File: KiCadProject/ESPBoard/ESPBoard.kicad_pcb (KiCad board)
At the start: 2 copper layers, 45 x 45 mm, 1 part, among them U301 ESP32-S3-WROOM-1

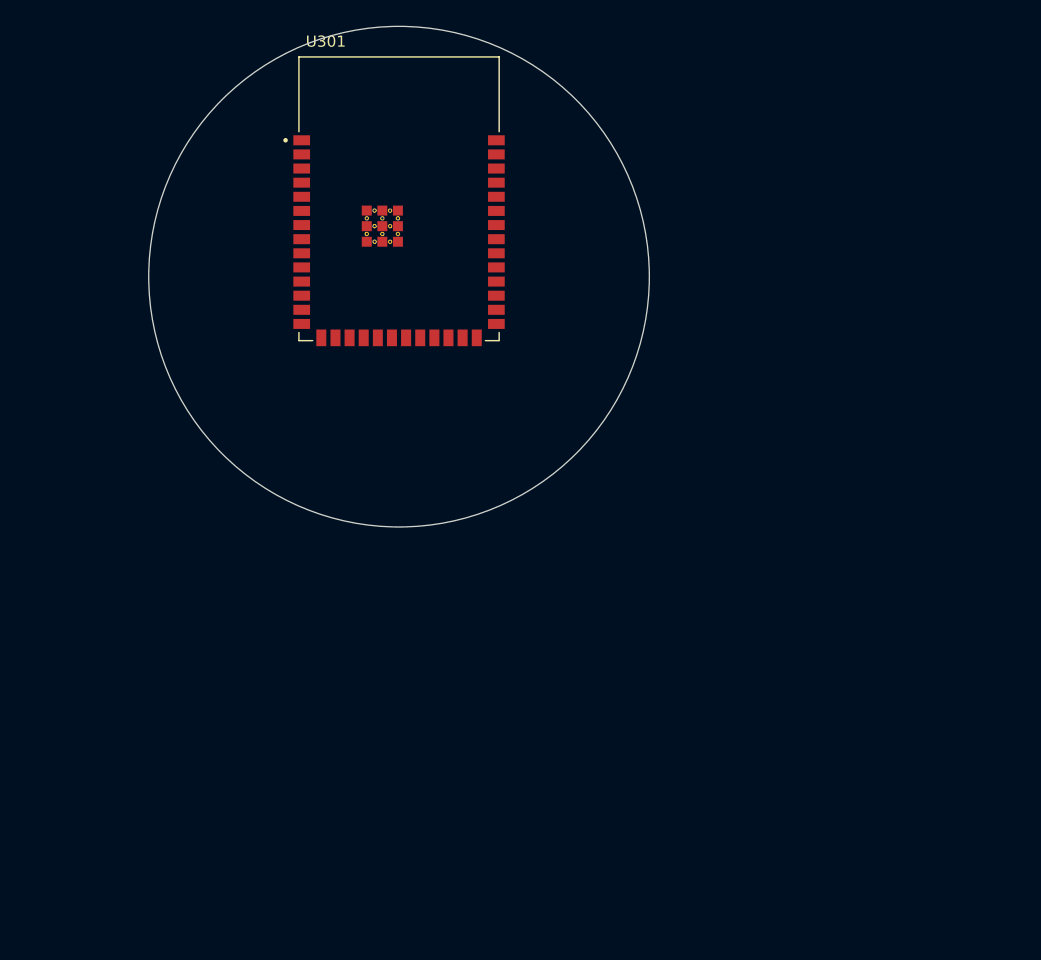
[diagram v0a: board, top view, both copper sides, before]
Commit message: ESP board layout mostly done. Small updates to battery management board
Signed-off-by: Eldalote.Electronics <Eldalote.Electronics@gmail.com>
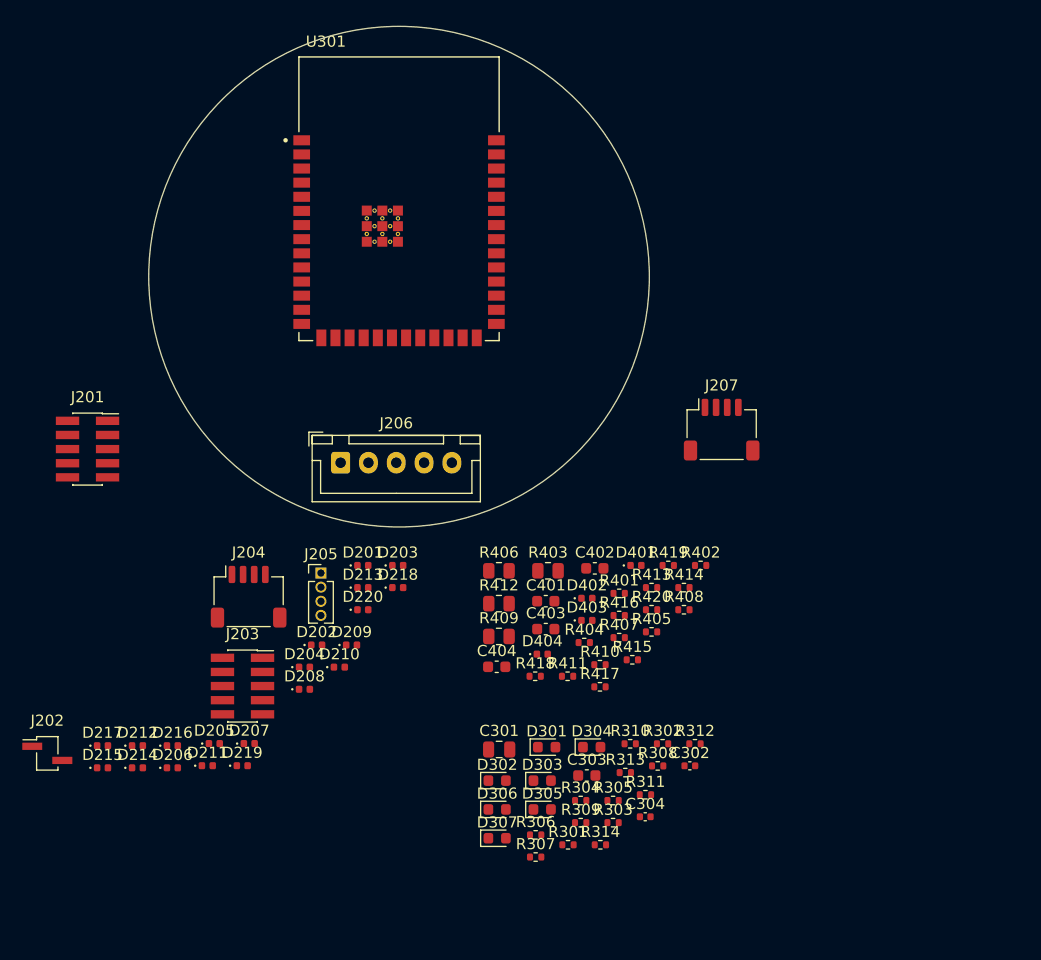
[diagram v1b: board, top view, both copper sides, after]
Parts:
- added C301: 10u, Capacitor_SMD:C_0805_2012Metric, F.Cu at (159.0, 142.5)
- added C302: 100n, Capacitor_SMD:C_0402_1005Metric, F.Cu at (176.1, 144.0)
- added C303: 1u, Capacitor_SMD:C_0603_1608Metric, F.Cu at (166.9, 144.8)
- added C304: 100n, Capacitor_SMD:C_0402_1005Metric, F.Cu at (172.1, 148.6)
- added C401: 1u, Capacitor_SMD:C_0603_1608Metric, F.Cu at (163.2, 129.2)
- added C402: 1u, Capacitor_SMD:C_0603_1608Metric, F.Cu at (167.6, 126.2)
- added C403: 1u, Capacitor_SMD:C_0603_1608Metric, F.Cu at (163.2, 131.7)
- added C404: 1u, Capacitor_SMD:C_0603_1608Metric, F.Cu at (158.8, 135.1)
- added D201: 3v3, Diode_SMD:D_0402_1005Metric, F.Cu at (146.7, 126.0)
- added D202: 3v3, Diode_SMD:D_0402_1005Metric, F.Cu at (142.6, 133.1)
- added D203: 3v3, Diode_SMD:D_0402_1005Metric, F.Cu at (149.9, 126.0)
- added D204: 3v3, Diode_SMD:D_0402_1005Metric, F.Cu at (141.5, 135.1)
- added D205: 3v3, Diode_SMD:D_0402_1005Metric, F.Cu at (133.4, 142.0)
- added D206: 3v3, Diode_SMD:D_0402_1005Metric, F.Cu at (129.6, 144.2)
- added D207: 3v3, Diode_SMD:D_0402_1005Metric, F.Cu at (136.5, 142.0)
- added D208: 3v3, Diode_SMD:D_0402_1005Metric, F.Cu at (141.5, 137.1)
- added D209: 3v3, Diode_SMD:D_0402_1005Metric, F.Cu at (145.7, 133.1)
- added D210: 3v3, Diode_SMD:D_0402_1005Metric, F.Cu at (144.6, 135.1)
- added D211: 3v3, Diode_SMD:D_0402_1005Metric, F.Cu at (132.8, 144.0)
- added D212: 3v3, Diode_SMD:D_0402_1005Metric, F.Cu at (126.5, 142.2)
- added D213: 3v3, Diode_SMD:D_0402_1005Metric, F.Cu at (146.7, 128.0)
- added D214: 3v3, Diode_SMD:D_0402_1005Metric, F.Cu at (126.5, 144.2)
- added D215: 3v3, Diode_SMD:D_0402_1005Metric, F.Cu at (123.3, 144.2)
- added D216: 3v3, Diode_SMD:D_0402_1005Metric, F.Cu at (129.6, 142.2)
- added D217: 3v3, Diode_SMD:D_0402_1005Metric, F.Cu at (123.3, 142.2)
- added D218: 3v3, Diode_SMD:D_0402_1005Metric, F.Cu at (149.9, 128.0)
- added D219: 3v3, Diode_SMD:D_0402_1005Metric, F.Cu at (135.9, 144.0)
- added D220: 3v3, Diode_SMD:D_0402_1005Metric, F.Cu at (146.7, 129.9)
- added D301: RED LED, LED_SMD:LED_0603_1608Metric, F.Cu at (163.3, 142.3)
- added D302: ORANGE LED, LED_SMD:LED_0603_1608Metric, F.Cu at (158.8, 145.3)
- added D303: GREEN LED, LED_SMD:LED_0603_1608Metric, F.Cu at (162.9, 145.3)
- added D304: GREEN LED, LED_SMD:LED_0603_1608Metric, F.Cu at (167.3, 142.3)
- added D305: GREEN LED, LED_SMD:LED_0603_1608Metric, F.Cu at (162.9, 147.9)
- added D306: GREEN LED, LED_SMD:LED_0603_1608Metric, F.Cu at (158.8, 147.9)
- added D307: GREEN LED, LED_SMD:LED_0603_1608Metric, F.Cu at (158.8, 150.5)
- added D401: 3v3, Diode_SMD:D_0402_1005Metric, F.Cu at (171.3, 126.0)
- added D402: 3v3, Diode_SMD:D_0402_1005Metric, F.Cu at (166.9, 128.9)
- added D403: 3v3, Diode_SMD:D_0402_1005Metric, F.Cu at (166.9, 130.9)
- added D404: 3v3, Diode_SMD:D_0402_1005Metric, F.Cu at (162.9, 133.9)
- added J201: Conn_02x05, Connector_PinSocket_1.27mm:PinSocket_2x05_P1.27mm_Vertical_SMD, F.Cu at (122.0, 115.5)
- added J202: Conn_01x02, Connector_PinSocket_1.27mm:PinSocket_1x02_P1.27mm_Vertical_SMD_Pin1Left, F.Cu at (118.4, 142.8)
- added J203: Conn_02x05, Connector_PinSocket_1.27mm:PinSocket_2x05_P1.27mm_Vertical_SMD, F.Cu at (135.9, 136.8)
- added J204: JST_SM04B, Connector_JST:JST_SH_SM04B-SRSS-TB_1x04-1MP_P1.00mm_Horizontal, F.Cu at (136.5, 128.8)
- added J205: DNP, Connector_PinHeader_1.27mm:PinHeader_1x04_P1.27mm_Vertical, F.Cu at (143.0, 126.6)
- added J206: JST_B5B_XH, Connector_JST:JST_XH_B5B-XH-A_1x05_P2.50mm_Vertical, F.Cu at (144.8, 116.7)
- added J207: JST_SM04B, Connector_JST:JST_SH_SM04B-SRSS-TB_1x04-1MP_P1.00mm_Horizontal, F.Cu at (179.0, 113.8)
- added R301: 10k, Resistor_SMD:R_0402_1005Metric, F.Cu at (165.2, 151.1)
- added R302: 100k, Resistor_SMD:R_0402_1005Metric, F.Cu at (173.7, 142.0)
- added R303: JMP, Resistor_SMD:R_0402_1005Metric, F.Cu at (169.2, 149.1)
- added R304: JMP, Resistor_SMD:R_0402_1005Metric, F.Cu at (166.3, 147.1)
- added R305: 100k, Resistor_SMD:R_0402_1005Metric, F.Cu at (169.2, 147.1)
- added R306: 100k, Resistor_SMD:R_0402_1005Metric, F.Cu at (162.3, 150.2)
- added R307: 100k, Resistor_SMD:R_0402_1005Metric, F.Cu at (162.3, 152.2)
- added R308: 240R, Resistor_SMD:R_0402_1005Metric, F.Cu at (173.2, 144.0)
- added R309: 240R, Resistor_SMD:R_0402_1005Metric, F.Cu at (166.3, 149.1)
- added R310: 240R, Resistor_SMD:R_0402_1005Metric, F.Cu at (170.8, 142.0)
- added R311: 240R, Resistor_SMD:R_0402_1005Metric, F.Cu at (172.2, 146.6)
- added R312: 240R, Resistor_SMD:R_0402_1005Metric, F.Cu at (176.6, 142.0)
- added R313: 240R, Resistor_SMD:R_0402_1005Metric, F.Cu at (170.3, 144.6)
- added R314: 240R, Resistor_SMD:R_0402_1005Metric, F.Cu at (168.1, 151.1)
- added R401: 10k, Resistor_SMD:R_0402_1005Metric, F.Cu at (169.8, 128.5)
- added R402: 10k, Resistor_SMD:R_0402_1005Metric, F.Cu at (177.1, 126.0)
- added R403: 100R, Resistor_SMD:R_0805_2012Metric, F.Cu at (163.4, 126.4)
- added R404: 10k, Resistor_SMD:R_0402_1005Metric, F.Cu at (166.7, 132.9)
- added R405: 10k, Resistor_SMD:R_0402_1005Metric, F.Cu at (172.7, 131.9)
- added R406: 100R, Resistor_SMD:R_0805_2012Metric, F.Cu at (159.0, 126.4)
- added R407: 10k, Resistor_SMD:R_0402_1005Metric, F.Cu at (169.8, 132.4)
- added R408: 10k, Resistor_SMD:R_0402_1005Metric, F.Cu at (175.6, 129.9)
- added R409: 100R, Resistor_SMD:R_0805_2012Metric, F.Cu at (159.0, 132.3)
- added R410: 10k, Resistor_SMD:R_0402_1005Metric, F.Cu at (168.1, 134.9)
- added R411: 10k, Resistor_SMD:R_0402_1005Metric, F.Cu at (165.2, 135.9)
- added R412: 100R, Resistor_SMD:R_0805_2012Metric, F.Cu at (159.0, 129.4)
- added R413: 10k, Resistor_SMD:R_0402_1005Metric, F.Cu at (172.7, 128.0)
- added R414: 19k1, Resistor_SMD:R_0402_1005Metric, F.Cu at (175.6, 128.0)
- added R415: 40k2, Resistor_SMD:R_0402_1005Metric, F.Cu at (171.0, 134.4)
- added R416: 19k1, Resistor_SMD:R_0402_1005Metric, F.Cu at (169.8, 130.5)
- added R417: 40k2, Resistor_SMD:R_0402_1005Metric, F.Cu at (168.1, 136.9)
- added R418: 10k, Resistor_SMD:R_0402_1005Metric, F.Cu at (162.2, 135.9)
- added R419: 10k, Resistor_SMD:R_0402_1005Metric, F.Cu at (174.2, 126.0)
- added R420: 10k, Resistor_SMD:R_0402_1005Metric, F.Cu at (172.7, 129.9)
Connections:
- U301 pad 1: unconnected-(U301-Pad1) -> GND
- U301 pad 12: unconnected-(U301-Pad12) -> BQ_CMPOUT
- U301 pad 13: unconnected-(U301-Pad13) -> /P3 ESP32/USB_D-
- U301 pad 14: unconnected-(U301-Pad14) -> /P3 ESP32/USB_D+
- U301 pad 15: unconnected-(U301-Pad15) -> /P3 ESP32/Select 3
- U301 pad 16: unconnected-(U301-Pad16) -> /P3 ESP32/Select 2
- U301 pad 2: unconnected-(U301-Pad2) -> +3.3V
- U301 pad 26: unconnected-(U301-Pad26) -> /P3 ESP32/Select 1
- U301 pad 27: unconnected-(U301-Pad27) -> /P3 ESP32/BOOT
- U301 pad 3: unconnected-(U301-Pad3) -> /P3 ESP32/CHIP_PU
- U301 pad 36: unconnected-(U301-Pad36) -> UART_RXDO
- U301 pad 37: unconnected-(U301-Pad37) -> UART_TXDO
- U301 pad 38: unconnected-(U301-Pad38) -> BQ_IADPT
- U301 pad 39: unconnected-(U301-Pad39) -> BQ_IBAT
- U301 pad 4: unconnected-(U301-Pad4) -> Cell1ADC
- U301 pad 40: unconnected-(U301-Pad40) -> GND
- U301 pad 5: unconnected-(U301-Pad5) -> Cell2ADC
- U301 pad 6: unconnected-(U301-Pad6) -> Cell3ADC
- U301 pad 7: unconnected-(U301-Pad7) -> Cell4ADC

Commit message: Tweaking
Signed-off-by: Eldalote.Electronics <Eldalote.Electronics@gmail.com>
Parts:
- removed D201, D202, D203, D204, D205, D206, D207, D208, D209, D210, D211, D212, D213, D214, D215, D216, D217, D218, D219, D220: 3v3, Diode_SMD:D_0402_1005Metric
- added Q401: NFET_Gatenames, Package_TO_SOT_SMD:SOT-23, B.Cu at (152.0, 88.5)
- added Q402: PMOS_Gatenames, Package_TO_SOT_SMD:SOT-23, B.Cu at (147.1, 88.5)
- added Q403: NFET_Gatenames, Package_TO_SOT_SMD:SOT-23, B.Cu at (156.9, 88.5)
- added Q404: PMOS_Gatenames, Package_TO_SOT_SMD:SOT-23, B.Cu at (142.2, 88.5)
- added Q405: NFET_Gatenames, Package_TO_SOT_SMD:SOT-23, B.Cu at (136.5, 88.2)
- added Q406: PMOS_Gatenames, Package_TO_SOT_SMD:SOT-23, B.Cu at (162.2, 85.8)
- added Q407: NFET_Gatenames, Package_TO_SOT_SMD:SOT-23, B.Cu at (136.5, 92.5)
- added Q408: PMOS_Gatenames, Package_TO_SOT_SMD:SOT-23, B.Cu at (163.0, 90.8)
- added R315: DNP, Resistor_SMD:R_0402_1005Metric, F.Cu at (189.7, 134.7)
- added R316: DNP, Resistor_SMD:R_0402_1005Metric, F.Cu at (183.0, 143.8)
- added R317: DNP, Resistor_SMD:R_0402_1005Metric, F.Cu at (163.2, 151.0)
- added REF**: USB-C cutout, Eldalote-footprints:USB-C cutout, F.Cu at (150.0, 114.5)
- added SW301: SW_Push, Button_Switch_SMD:SW_Push_1P1T_NO_6x6mm_H9.5mm, F.Cu at (167.8, 99.5)
- added SW302: SW_Push, Button_Switch_SMD:SW_Push_1P1T_NO_6x6mm_H9.5mm, F.Cu at (132.5, 99.8)
- J201, J202, J203, J204, J207: moved to B.Cu
- J205: footprint Connector_PinHeader_1.27mm:PinHeader_1x04_P1.27mm_Vertical -> Connector_PinHeader_1.27mm:PinHeader_2x02_P1.27mm_Vertical_SMD
- J206: value JST_B5B_XH -> 1x05 female; footprint Connector_JST:JST_XH_B5B-XH-A_1x05_P2.50mm_Vertical -> Connector_PinSocket_1.27mm:PinSocket_1x05_P1.27mm_Vertical_SMD_Pin1Left; moved to B.Cu
- moved J203 49.4 mm to (168.2, 99.5), turned to 180 degrees
- moved J202 47.1 mm to (150.0, 108.0), turned to -90 degrees
- moved R307 44.5 mm to (203.5, 135.5)
- moved D307 42.0 mm to (158.8, 108.5), turned to -90 degrees
- moved D305 40.6 mm to (153.0, 108.5), turned to -90 degrees
- moved D301 40.3 mm to (141.2, 108.5), turned to -90 degrees
- moved D303 40.0 mm to (147.2, 108.5), turned to -90 degrees
- moved D302 39.6 mm to (144.2, 108.5), turned to -90 degrees
- moved D306 39.5 mm to (156.0, 108.5), turned to -90 degrees
- moved D304 38.0 mm to (150.0, 108.5), turned to -90 degrees
- moved R313 36.3 mm to (156.0, 111.2), turned to 90 degrees
- moved J206 34.9 mm to (150.0, 82.2), turned to -90 degrees
- moved R306 33.4 mm to (138.2, 127.0)
- moved R301 31.9 mm to (192.6, 134.7)
- moved R309 27.9 mm to (194.0, 145.8)
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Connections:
- net /P3 ESP32/BOOT renamed /P3 ESP32/BOOT/USER1
- net Net-(D301-Pad2) renamed /P3 ESP32/L0a
- net Net-(D302-Pad2) renamed /P3 ESP32/L1a
- net Net-(D303-Pad2) renamed /P3 ESP32/L2a
- net Net-(D304-Pad2) renamed /P3 ESP32/L3a
- net Net-(D305-Pad2) renamed /P3 ESP32/L4a
- net Net-(D306-Pad2) renamed /P3 ESP32/L5a
- net Net-(D307-Pad2) renamed /P3 ESP32/L6a

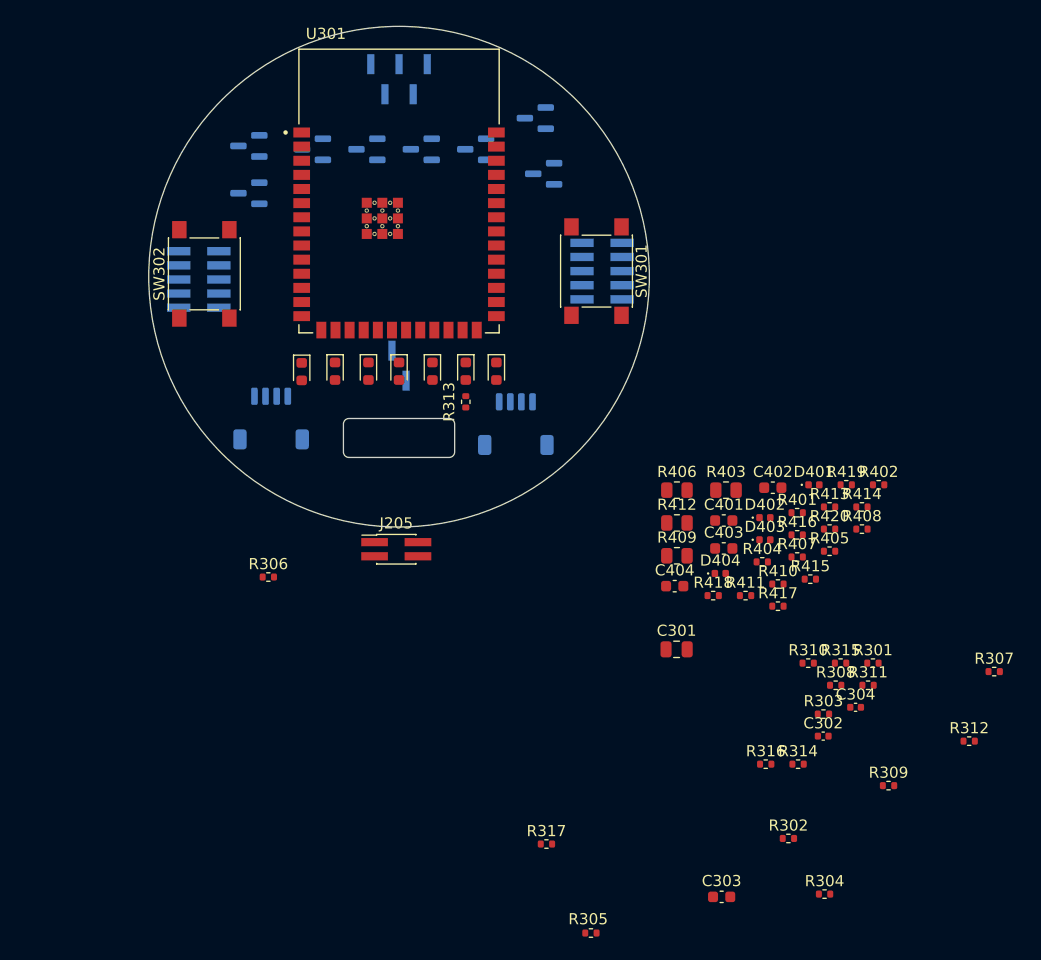
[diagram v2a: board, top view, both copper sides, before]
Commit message: Components selected, MfID added to schematics, and components ordered
Signed-off-by: Eldalote.Electronics <Eldalote.Electronics@gmail.com>
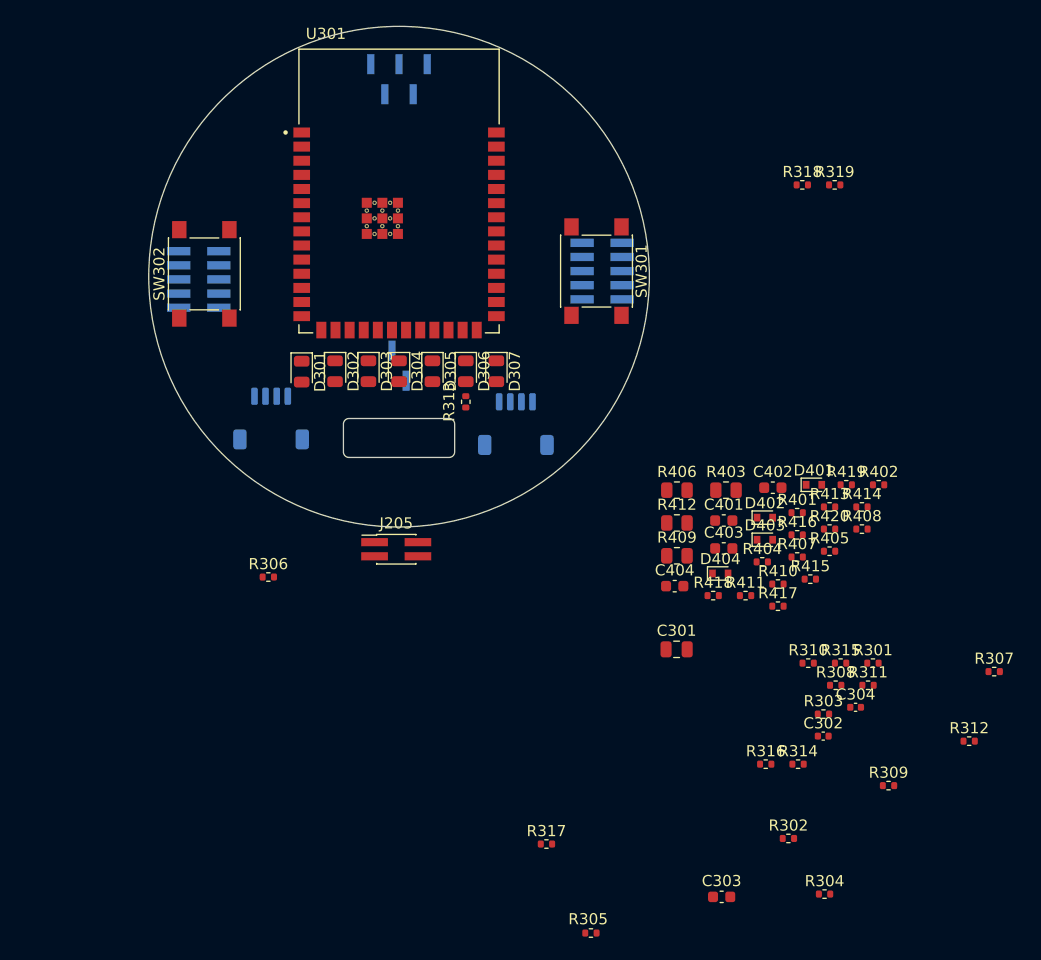
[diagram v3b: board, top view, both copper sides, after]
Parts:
- removed Q401, Q403, Q405, Q407: NFET_Gatenames, Package_TO_SOT_SMD:SOT-23
- removed Q402, Q404, Q406, Q408: PMOS_Gatenames, Package_TO_SOT_SMD:SOT-23
- added R318: 5k1, Resistor_SMD:R_0402_1005Metric, F.Cu at (186.2, 91.8)
- added R319: 5k1, Resistor_SMD:R_0402_1005Metric, F.Cu at (189.2, 91.8)
- D301, D302, D303, D304, D305, D306, D307: footprint LED_SMD:LED_0603_1608Metric -> LED_SMD:LED_0805_2012Metric
- D401, D402, D403, D404: footprint Diode_SMD:D_0402_1005Metric -> Diode_SMD:D_SOD-523
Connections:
- J204 pad 1: GND -> +3V3

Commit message: Layout on the battery management board
Signed-off-by: Eldalote.Electronics <Eldalote.Electronics@gmail.com>
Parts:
- moved REF** 13.8 mm to (163.0, 110.0), turned to 90 degrees
- moved J207 10.4 mm to (150.8, 117.0)
- moved J206 6.25 mm to (149.8, 88.5)
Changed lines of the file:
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@@
   )
   (footprint "Eldalote-footprints:USB-C cutout" (layer "F.Cu")
-    (at 150 114.5)
-    (attr smd)
-    (fp_text reference "REF**" (at 0.1 -2.55 unlocked) (layer "Dwgs.User")
-      (effects (font (size 1 1) (thickness 0.15)))
-    )
-    (fp_text value "USB-C cutout" (at 0.2 3 unlocked) (layer "F.Fab")
-      (effects (font (size 1 1) (thickness 0.15)))
-    )
-    (fp_text user "${REFERENCE}" (at 0.2 4.5 unlocked) (layer "F.Fab")
+    (at 163 110 90)
+    (attr smd)
+    (fp_text reference "REF**" (at 0.1 -2.55 90 unlocked) (layer "Dwgs.User")
+      (effects (font (size 1 1) (thickness 0.15)))
+    )
+    (fp_text value "USB-C cutout" (at 0.2 3 90 unlocked) (layer "F.Fab")
+      (effects (font (size 1 1) (thickness 0.15)))
+    )
+    (fp_text user "${REFERENCE}" (at 0.2 4.5 90 unlocked) (layer "F.Fab")
       (effects (font (size 1 1) (thickness 0.15)))
     )
@@
   )
   (footprint "Connector_JST:JST_SH_SM04B-SRSS-TB_1x04-1MP_P1.00mm_Horizontal" (layer "B.Cu")
-    (at 160.5 113.25 180)
+    (at 150.75 117 180)
     (descr "JST SH series connector, SM04B-SRSS-TB (http://www.jst-mfg.com/product/pdf/eng/eSH.pdf), generated with kicad-footprint-generator")
     (tags "connector JST SH top entry")
@@
   )
   (footprint "Connector_PinSocket_1.27mm:PinSocket_1x05_P1.27mm_Vertical_SMD_Pin1Left" (layer "B.Cu")
-    (at 150 82.25 -90)
+    (at 149.75 88.5 -90)
     (descr "surface-mounted straight socket strip, 1x05, 1.27mm pitch, single row, style 1 (pin 1 left) (https://gct.co/pdfjs/web/viewer.html?file=/Files/Drawings/BD075.pdf&t=1511594726925), script generated")
     (tags "Surface mounted socket strip SMD 1x05 1.27mm single row style1 pin1 left")
